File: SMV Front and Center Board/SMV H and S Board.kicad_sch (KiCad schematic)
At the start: 69 parts, among them J1 430450200, J10 Molex Micro-Fit 4 Pin, J2 430450200, J4 22035035, J5 22035035, J6 22035035, J7 22035035, J8 430450200, Q1 PSMN1R8-40YLC_115, Q2 PSMN1R8-40YLC_115, U1 UA78M05QDCYRG4Q1, U2 MCP6286T-E/OT, U3 PADS131M04QPWRQ1, U4 MCP6286T-E/OT

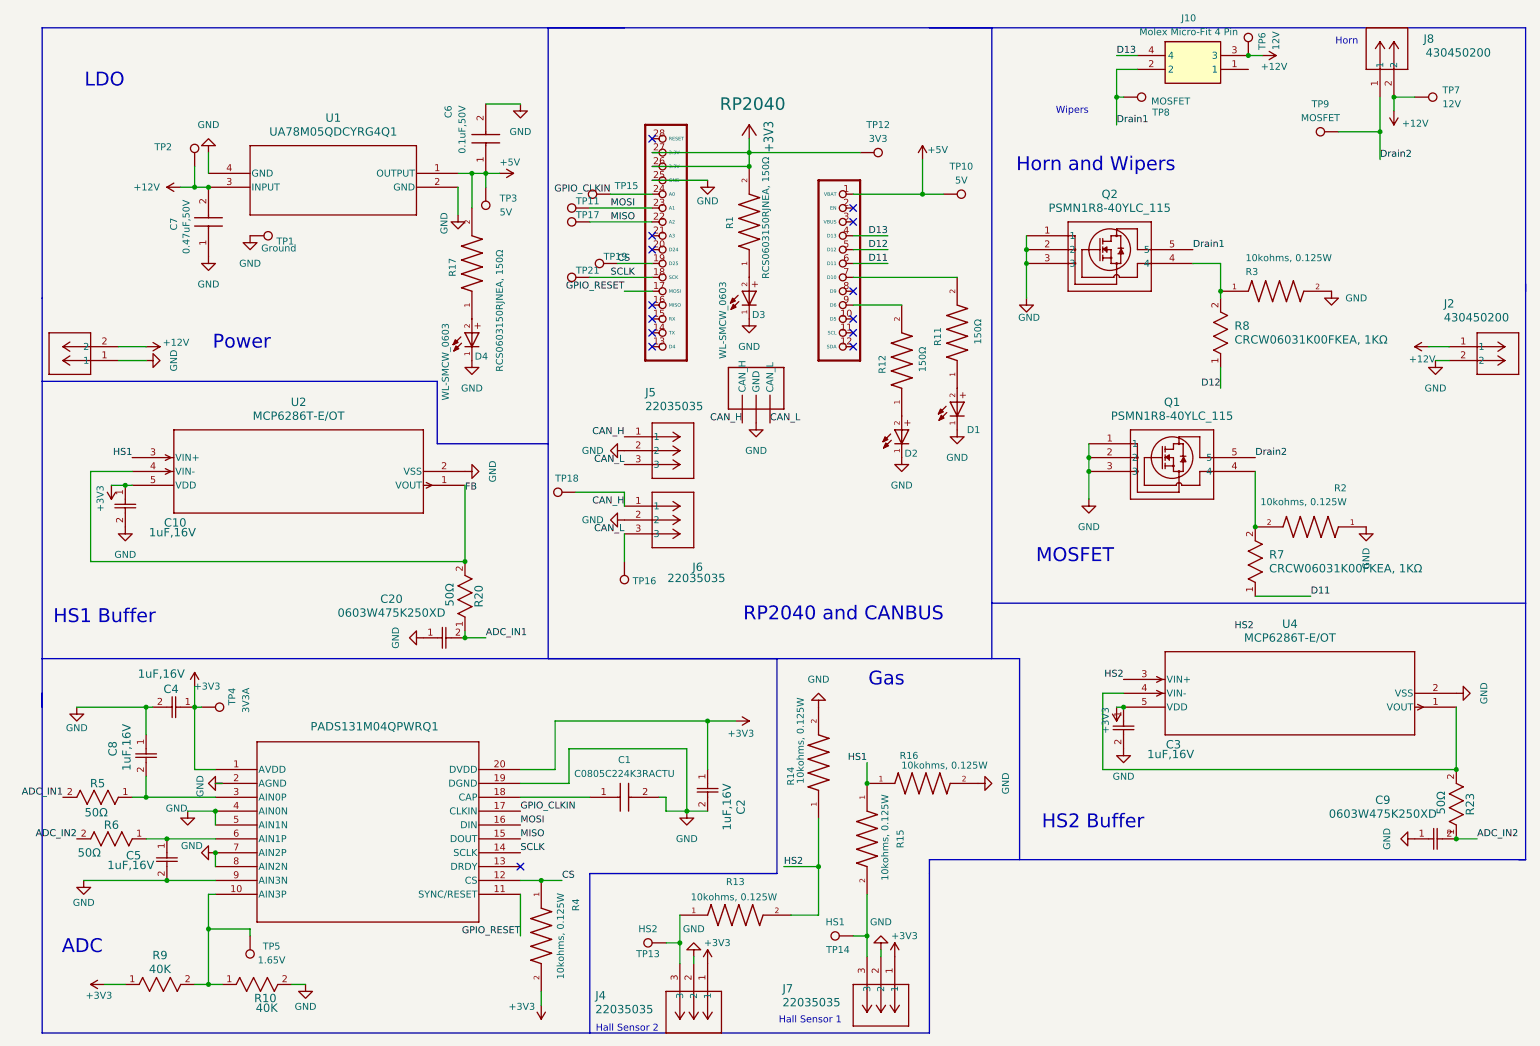
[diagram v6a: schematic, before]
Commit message: Added ground connections and finalized CAN
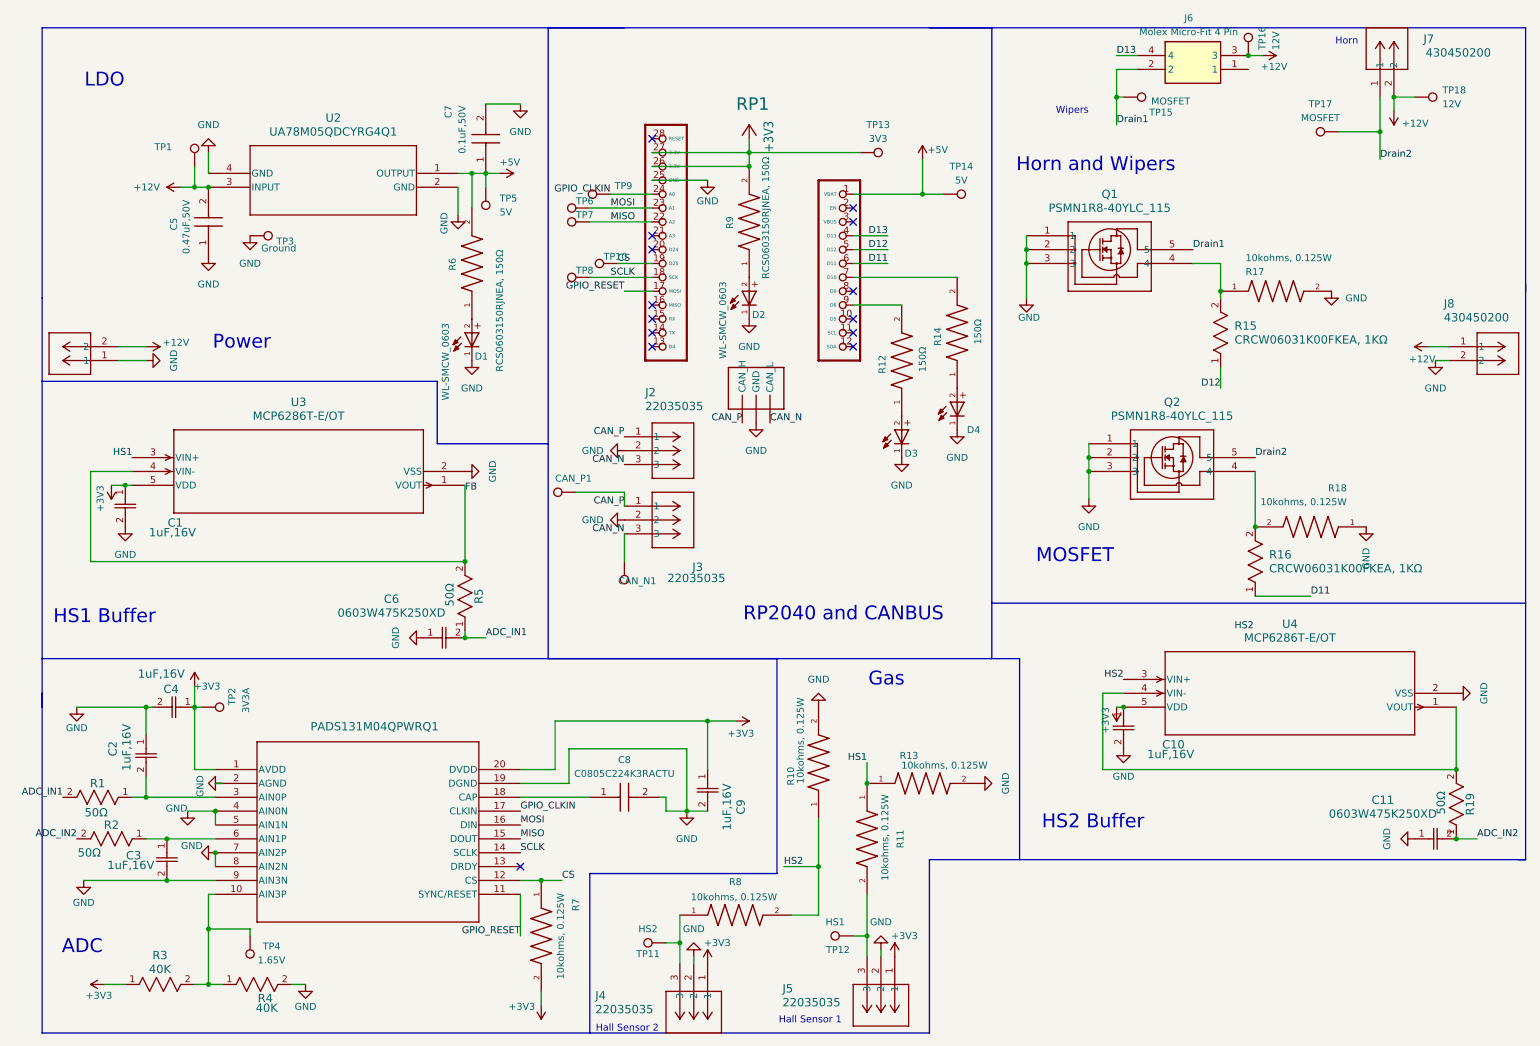
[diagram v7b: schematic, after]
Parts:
- renumbered C10 to C1, C3 to C10, C9 to C11, C8 to C2, C5 to C3, C7 to C5, C20 to C6, C6 to C7, C1 to C8, C2 to C9, TP16 to CAN_N1, TP18 to CAN_P1, D4 to D1, D3 to D2, D2 to D3, D1 to D4, J5 to J2, J6 to J3, J7 to J5, J10 to J6, J8 to J7, J2 to J8, Q2 to Q1, Q1 to Q2, R5 to R1, R14 to R10, R15 to R11, R16 to R13, R11 to R14, R8 to R15, R7 to R16, R3 to R17, R2 to R18, R23 to R19, R6 to R2, R9 to R3, R10 to R4, R20 to R5, R17 to R6, R4 to R7, R13 to R8, R1 to R9, RP2040 to RP1, TP2 to TP1, TP19 to TP10, TP13 to TP11, TP14 to TP12, TP12 to TP13, TP10 to TP14, TP8 to TP15, TP6 to TP16, TP9 to TP17, TP7 to TP18, TP4 to TP2, TP1 to TP3, TP5 to TP4, TP3 to TP5, TP11 to TP6, TP17 to TP7, TP21 to TP8, TP15 to TP9, U3 to U1, U1 to U2, U2 to U3
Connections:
- net CAN_H renamed CAN_P
- net CAN_L renamed CAN_N

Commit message: Finalized layout
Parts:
- removed TP14: 5V, TestPoint:TestPoint_Pad_D3.0mm, symbol Connector:TestPoint
- removed TP16, TP18: 12V, TestPoint:TestPoint_Pad_D3.0mm, symbol Connector:TestPoint
- removed TP2: 3V3A, TestPoint:TestPoint_Pad_D3.0mm, symbol Connector:TestPoint
